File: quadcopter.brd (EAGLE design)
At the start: 143.4 x 143.4 mm, 69 parts, among them J1 AVR_SPI_PRG_6NS, U1 ATMEGA128RFA1, Y2 16MHz

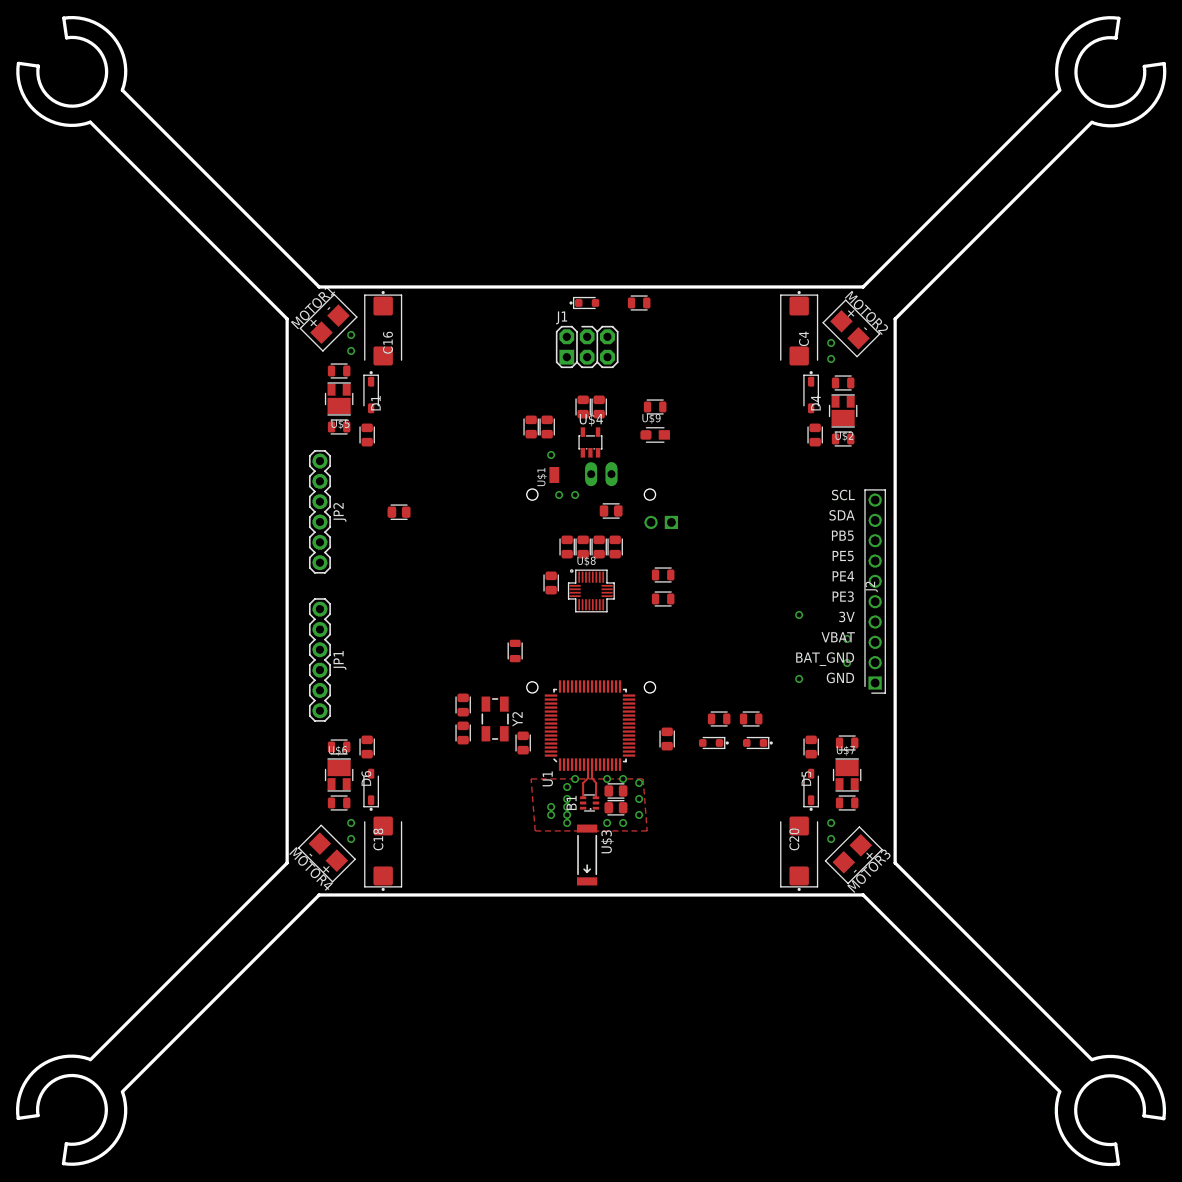
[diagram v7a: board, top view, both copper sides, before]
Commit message: Fixed motor holder and arm dimensions (now fits within bounding box
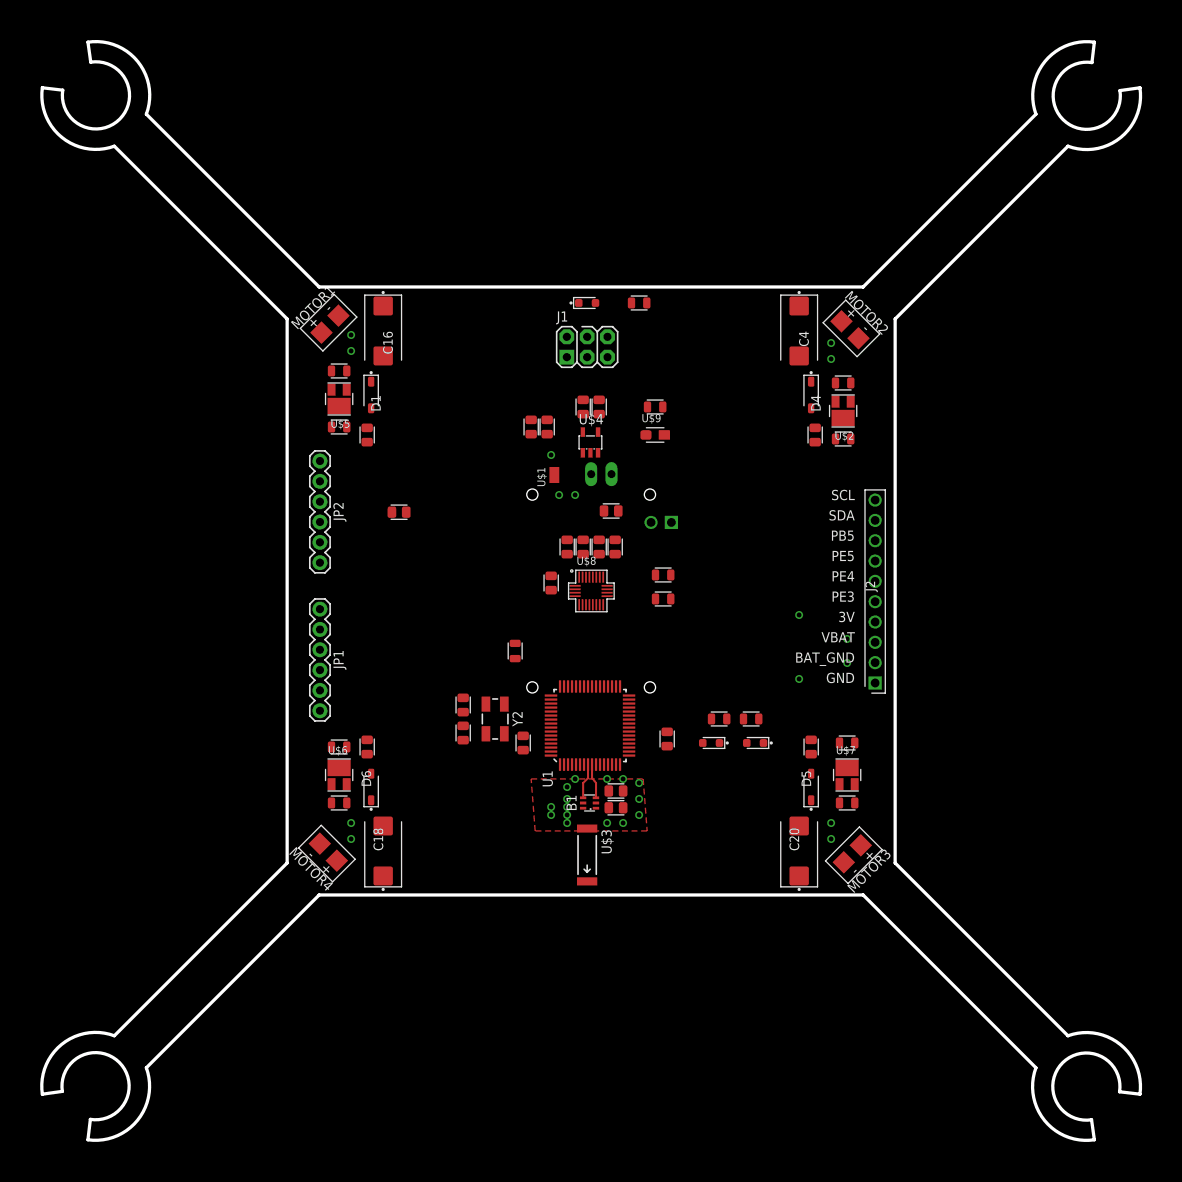
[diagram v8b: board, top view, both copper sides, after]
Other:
- board size 143.4 x 143.4 mm -> 137.3 x 137.3 mm
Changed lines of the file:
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@@
 <setting verticaltext="up"/>
 </settings>
-<grid distance="0.5" unitdist="mm" unit="mm" style="lines" multiple="1" display="yes" altdistance="0.025" altunitdist="inch" altunit="inch"/>
+<grid distance="1" unitdist="mm" unit="mm" style="lines" multiple="1" display="yes" altdistance="0.025" altunitdist="inch" altunit="inch"/>
 <layers>
 <layer number="1" name="Top" color="4" fill="1" visible="yes" active="yes"/>
@@
 <board>
 <plain>
-<wire x1="107.1421375" y1="103.5710625" x2="103.60660625" y2="107.1066" width="0.4064" layer="20" curve="-288.924644"/>
-<wire x1="109.6170125" y1="103.924615625" x2="100.778178125" y2="96.499996875" width="0.4064" layer="20" curve="-117.407575"/>
-<wire x1="96.535540625" y1="100.7426375" x2="103.960159375" y2="109.581471875" width="0.4064" layer="20" curve="-117.407575"/>
-<wire x1="103.960159375" y1="109.581471875" x2="103.60660625" y2="107.1066" width="0.4064" layer="20"/>
-<wire x1="107.1421375" y1="103.5710625" x2="109.6170125" y2="103.924615625" width="0.4064" layer="20"/>
-<wire x1="96.6" y1="100.6" x2="72" y2="76" width="0.4064" layer="20"/>
-<wire x1="100.6" y1="96.6" x2="76" y2="72" width="0.4064" layer="20"/>
-<wire x1="-27.5710625" y1="107.1421375" x2="-31.1066" y2="103.60660625" width="0.4064" layer="20" curve="-288.924644"/>
-<wire x1="-33.581471875" y1="103.960159375" x2="-31.1066" y2="103.60660625" width="0.4064" layer="20"/>
-<wire x1="-27.5710625" y1="107.1421375" x2="-27.924615625" y2="109.6170125" width="0.4064" layer="20"/>
-<wire x1="-24.6" y1="96.6" x2="0" y2="72" width="0.4064" layer="20"/>
-<wire x1="-20.6" y1="100.6" x2="4" y2="76" width="0.4064" layer="20"/>
-<wire x1="-31.1421375" y1="-27.5710625" x2="-27.60660625" y2="-31.1066" width="0.4064" layer="20" curve="-288.924644"/>
-<wire x1="-33.6170125" y1="-27.924615625" x2="-24.778178125" y2="-20.499996875" width="0.4064" layer="20" curve="-117.407575"/>
-<wire x1="-20.535540625" y1="-24.7426375" x2="-27.960159375" y2="-33.581471875" width="0.4064" layer="20" curve="-117.407575"/>
-<wire x1="-27.960159375" y1="-33.581471875" x2="-27.60660625" y2="-31.1066" width="0.4064" layer="20"/>
-<wire x1="-31.1421375" y1="-27.5710625" x2="-33.6170125" y2="-27.924615625" width="0.4064" layer="20"/>
-<wire x1="-20.6" y1="-24.6" x2="4" y2="0" width="0.4064" layer="20"/>
-<wire x1="-24.6" y1="-20.6" x2="0" y2="4" width="0.4064" layer="20"/>
-<wire x1="103.5710625" y1="-31.1421375" x2="107.1066" y2="-27.60660625" width="0.4064" layer="20" curve="-288.924644"/>
-<wire x1="103.924615625" y1="-33.6170125" x2="96.499996875" y2="-24.778178125" width="0.4064" layer="20" curve="-117.407575"/>
-<wire x1="100.7426375" y1="-20.535540625" x2="109.581471875" y2="-27.960159375" width="0.4064" layer="20" curve="-117.407575"/>
-<wire x1="109.581471875" y1="-27.960159375" x2="107.1066" y2="-27.60660625" width="0.4064" layer="20"/>
-<wire x1="103.5710625" y1="-31.1421375" x2="103.924615625" y2="-33.6170125" width="0.4064" layer="20"/>
-<wire x1="100.6" y1="-20.6" x2="76" y2="4" width="0.4064" layer="20"/>
-<wire x1="96.6" y1="-24.6" x2="72" y2="0" width="0.4064" layer="20"/>
-<wire x1="-27.9" y1="109.6" x2="-20.6" y2="100.6" width="0.4064" layer="20" curve="-119.008144"/>
-<wire x1="-24.6" y1="96.6" x2="-33.6" y2="103.9" width="0.4064" layer="20" curve="-117.980858"/>
+<wire x1="-21.6" y1="93.6" x2="0" y2="72" width="0.4064" layer="20"/>
+<wire x1="-17.6" y1="97.6" x2="4" y2="76" width="0.4064" layer="20"/>
+<wire x1="-24.9" y1="106.6" x2="-17.6" y2="97.6" width="0.4064" layer="20" curve="-119.008144"/>
+<wire x1="-21.6" y1="93.6" x2="-30.6" y2="100.9" width="0.4064" layer="20" curve="-117.980858"/>
 <wire x1="4" y1="76" x2="72" y2="76" width="0.4064" layer="20"/>
 <wire x1="76" y1="4" x2="76" y2="72" width="0.4064" layer="20"/>
@@
 <vertex x="30" y="15"/>
 </polygon>
+<wire x1="-24.55" y1="104.1" x2="-28.05" y2="100.6" width="0.4064" layer="20" curve="-287.803432"/>
+<wire x1="-30.6" y1="100.9" x2="-28.05" y2="100.6" width="0.4064" layer="20"/>
+<wire x1="-24.9" y1="106.6" x2="-24.55" y2="104.1" width="0.4064" layer="20"/>
+<wire x1="93.6" y1="97.6" x2="72" y2="76" width="0.4064" layer="20"/>
+<wire x1="97.6" y1="93.6" x2="76" y2="72" width="0.4064" layer="20"/>
+<wire x1="106.6" y1="100.9" x2="97.6" y2="93.6" width="0.4064" layer="20" curve="-119.008144"/>
+<wire x1="93.6" y1="97.6" x2="100.9" y2="106.6" width="0.4064" layer="20" curve="-117.980858"/>
+<wire x1="104.1" y1="100.55" x2="100.6" y2="104.05" width="0.4064" layer="20" curve="-287.803432"/>
+<wire x1="100.9" y1="106.6" x2="100.6" y2="104.05" width="0.4064" layer="20"/>
+<wire x1="106.6" y1="100.9" x2="104.1" y2="100.55" width="0.4064" layer="20"/>
+<wire x1="-17.6" y1="-21.6" x2="4" y2="0" width="0.4064" layer="20"/>
+<wire x1="-21.6" y1="-17.6" x2="0" y2="4" width="0.4064" layer="20"/>
+<wire x1="-30.6" y1="-24.9" x2="-21.6" y2="-17.6" width="0.4064" layer="20" curve="-119.008144"/>
+<wire x1="-17.6" y1="-21.6" x2="-24.9" y2="-30.6" width="0.4064" layer="20" curve="-117.980858"/>
+<wire x1="-28.1" y1="-24.55" x2="-24.6" y2="-28.05" width="0.4064" layer="20" curve="-287.803432"/>
+<wire x1="-24.9" y1="-30.6" x2="-24.6" y2="-28.05" width="0.4064" layer="20"/>
+<wire x1="-30.6" y1="-24.9" x2="-28.1" y2="-24.55" width="0.4064" layer="20"/>
+<wire x1="97.6" y1="-17.6" x2="76" y2="4" width="0.4064" layer="20"/>
+<wire x1="93.6" y1="-21.6" x2="72" y2="0" width="0.4064" layer="20"/>
+<wire x1="100.9" y1="-30.6" x2="93.6" y2="-21.6" width="0.4064" layer="20" curve="-119.008144"/>
+<wire x1="97.6" y1="-17.6" x2="106.6" y2="-24.9" width="0.4064" layer="20" curve="-117.980858"/>
+<wire x1="100.55" y1="-28.1" x2="104.05" y2="-24.6" width="0.4064" layer="20" curve="-287.803432"/>
+<wire x1="106.6" y1="-24.9" x2="104.05" y2="-24.6" width="0.4064" layer="20"/>
+<wire x1="100.9" y1="-30.6" x2="100.55" y2="-28.1" width="0.4064" layer="20"/>
 </plain>
 <attributes>
